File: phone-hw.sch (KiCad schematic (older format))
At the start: 39 parts, among them J1 USB_C_Receptacle_USB2.0, J2 Conn_01x06, J3 Conn_01x05, Q1 S9015, SW1 SW_Push, SW2 SW_Push, SW3 TSWB-3N-CB, U1 ESP32-WROVER, U11 NSI45015WT1G, U2 MCP23008_SO, U3 XC6222B281MR-G, U4 NVT2008, U5 ER-TFT1.44-1, U6 L80-R

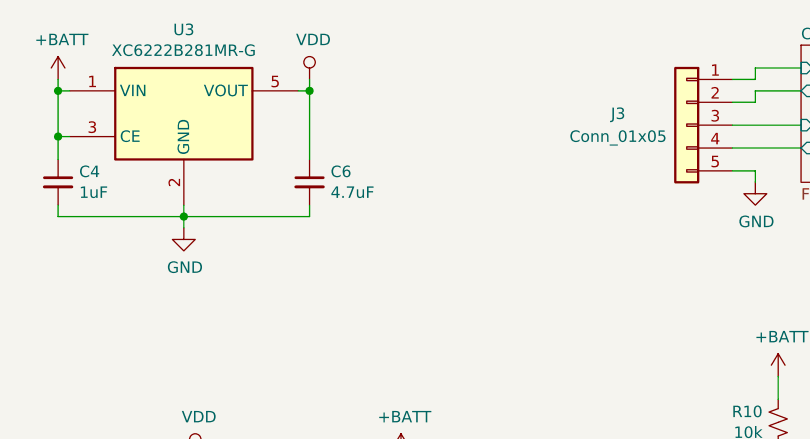
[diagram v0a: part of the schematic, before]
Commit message: add some extra capacitance to the 2.8v line
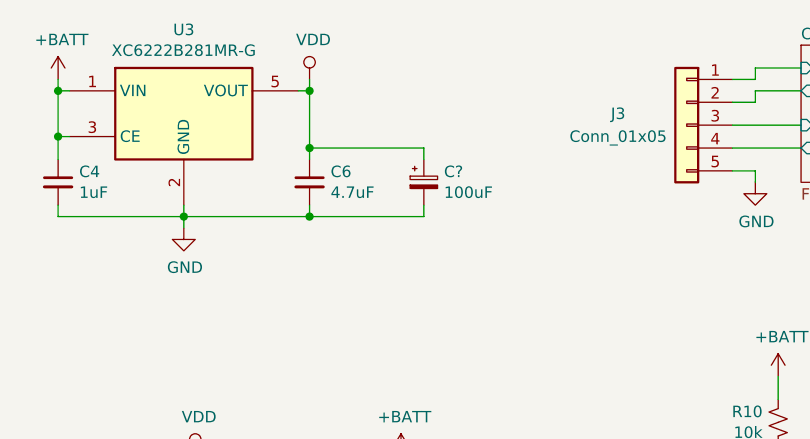
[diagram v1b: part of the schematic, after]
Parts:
- added C?: 100uF, Capacitor_Tantalum_SMD:CP_EIA-3528-15_AVX-H_Pad1.50x2.35mm_HandSolder, symbol Device:CP_Small
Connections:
- net GND: now also C?.2
- net VDD: now also C?.1
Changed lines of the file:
@@
 	6300 1550 6300 1500
 Wire Wire Line
-	6300 1300 6300 1000
+	6300 1300 6300 1250
 Connection ~ 6300 1000
 $Comp
@@
 Wire Wire Line
 	3100 6000 3250 6000
+Wire Wire Line
+	6300 1550 6800 1550
+Wire Wire Line
+	6800 1550 6800 1500
+Connection ~ 6300 1550
+Wire Wire Line
+	6300 1250 6800 1250
+Wire Wire Line
+	6800 1250 6800 1300
+Connection ~ 6300 1250
+Wire Wire Line
+	6300 1250 6300 1000
+$Comp
+L Device:CP_Small C?
+U 1 1 5CE0C170
+P 6800 1400
+F 0 "C?" H 6888 1446 50  0000 L CNN
+F 1 "100uF" H 6888 1355 50  0000 L CNN
+F 2 "Capacitor_Tantalum_SMD:CP_EIA-3528-15_AVX-H_Pad1.50x2.35mm_HandSolder" H 6800 1400 50  0001 C CNN
+F 3 "~" H 6800 1400 50  0001 C CNN
+	1    6800 1400
+	1    0    0    -1
+$EndComp
 $EndSCHEMATC

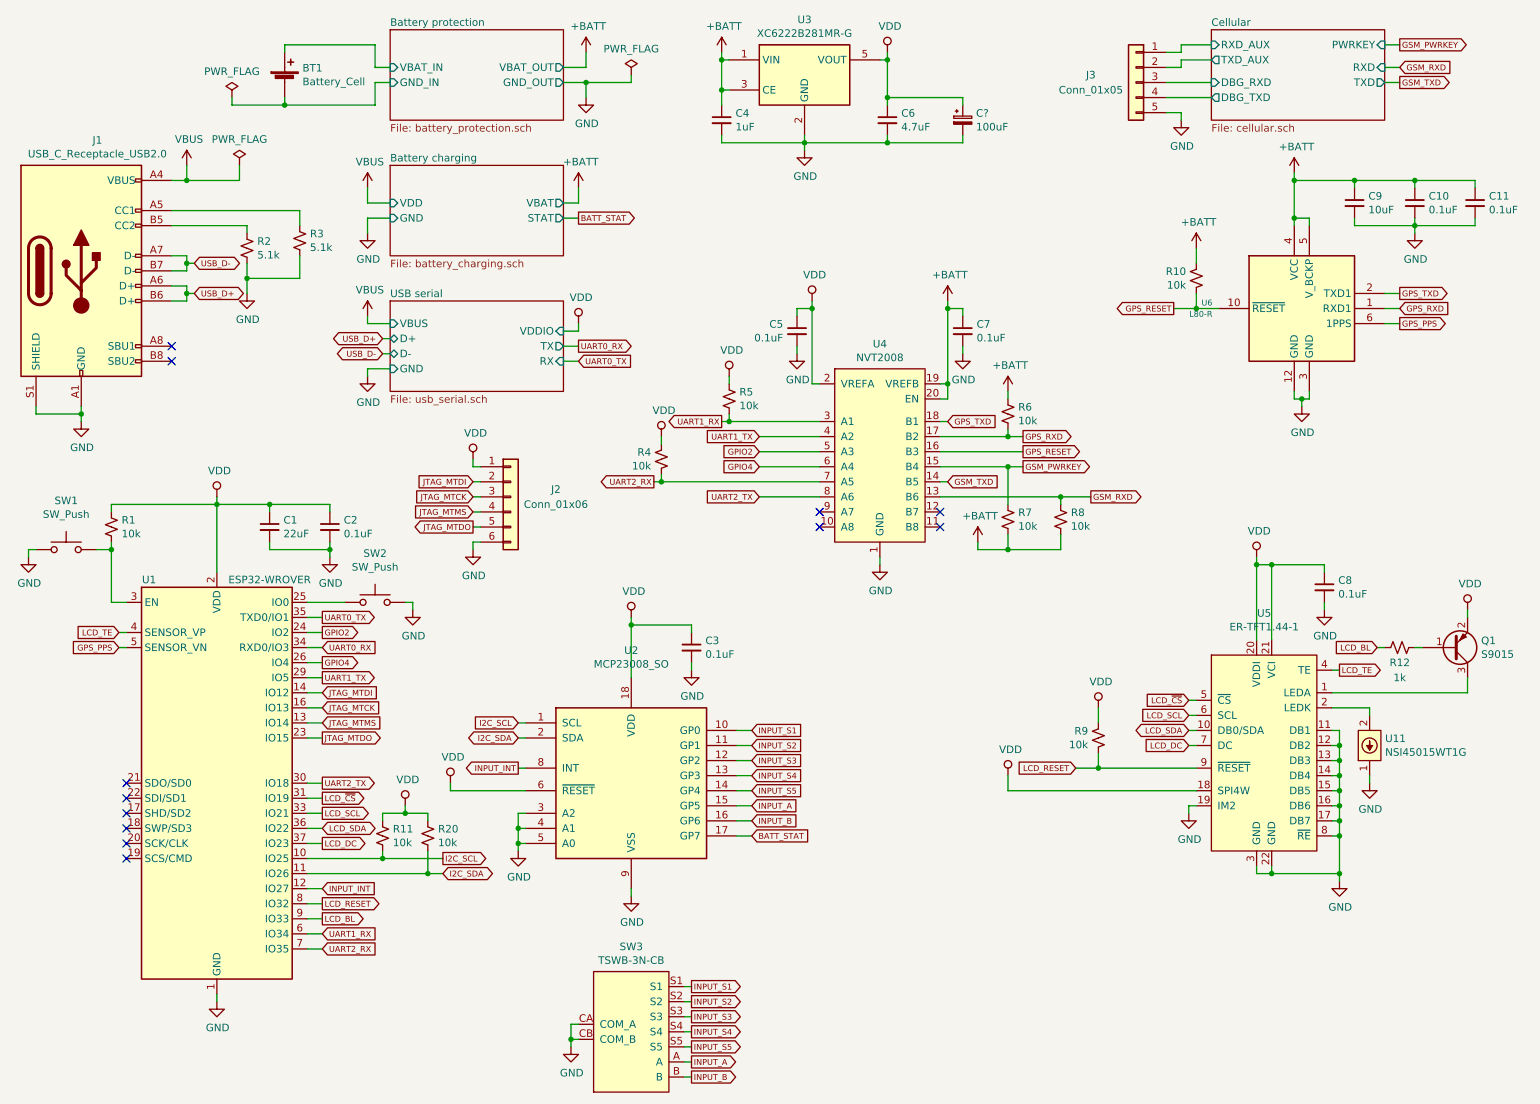
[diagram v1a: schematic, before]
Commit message: clear existing annotations from schematic
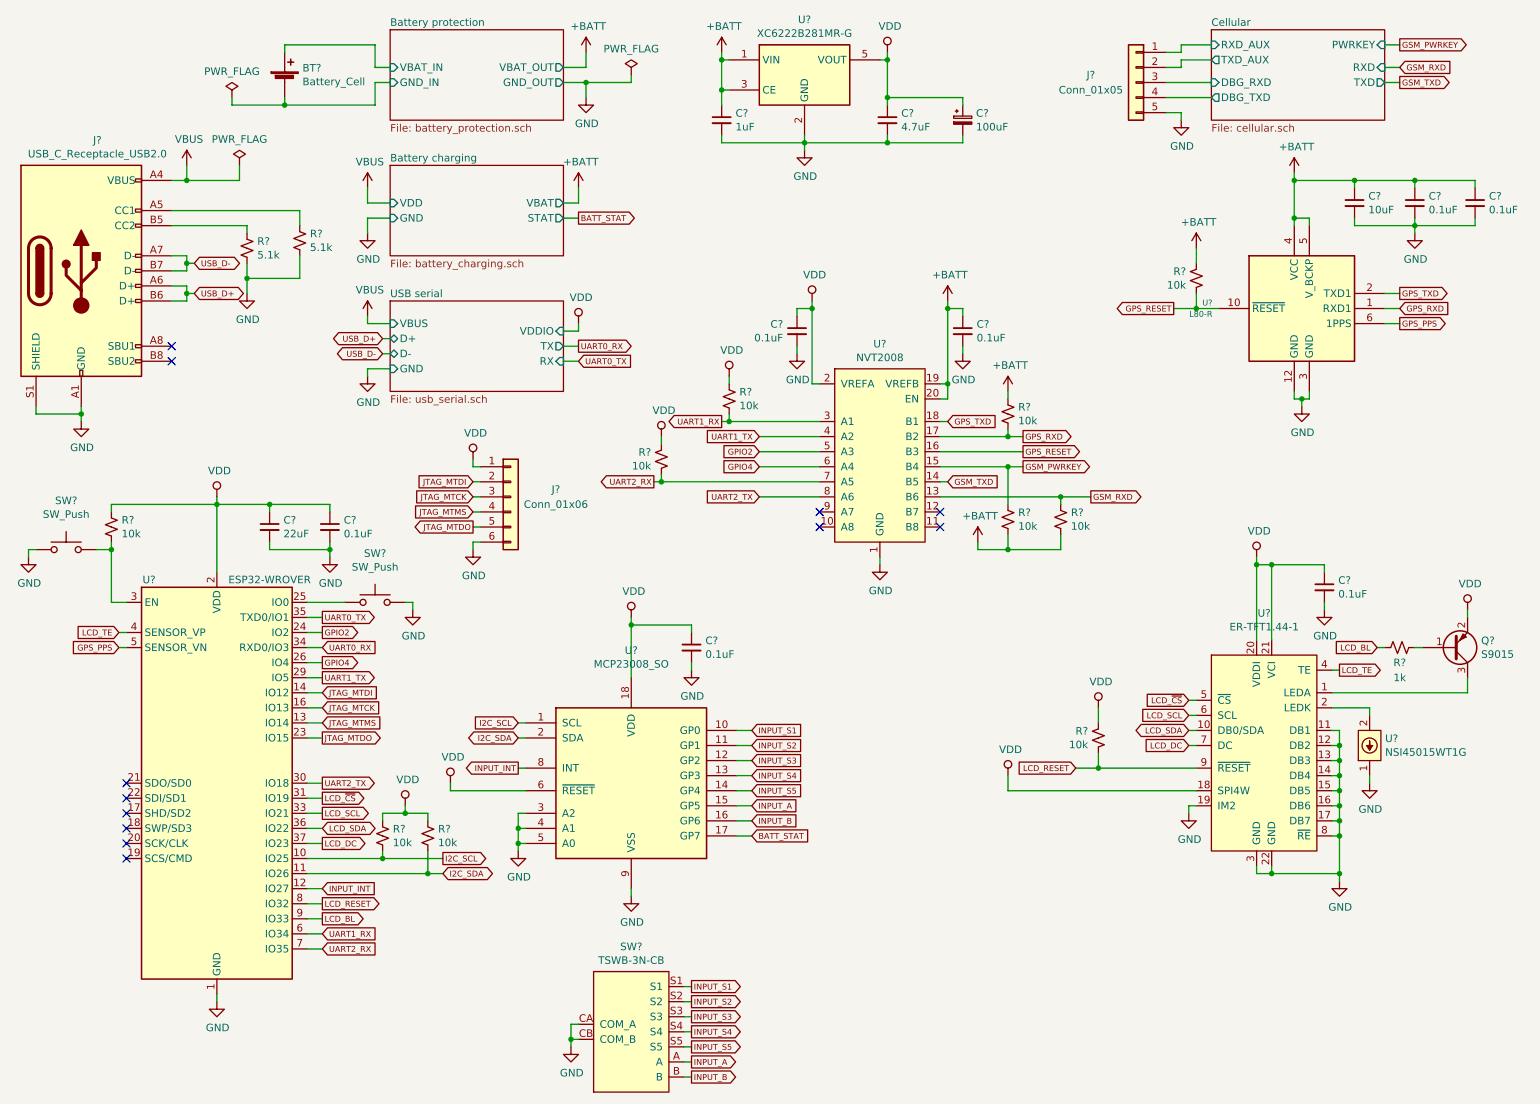
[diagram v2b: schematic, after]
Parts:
- renumbered BT1 to BT?, C4 to C?, C6 to C?, C1 to C?, C2 to C?, C8 to C?, C9 to C?, C10 to C?, C11 to C?, C3 to C?, C5 to C?, C7 to C?, J1 to J?, J3 to J?, J2 to J?, Q1 to Q?, R2 to R?, R3 to R?, R1 to R?, R9 to R?, R10 to R?, R5 to R?, R6 to R?, R7 to R?, R8 to R?, R4 to R?, R12 to R?, R11 to R?, R20 to R?, SW1 to SW?, SW2 to SW?, SW3 to SW?, U3 to U?, U1 to U?, U5 to U?, U4 to U?, U6 to U?, U2 to U?, U11 to U?

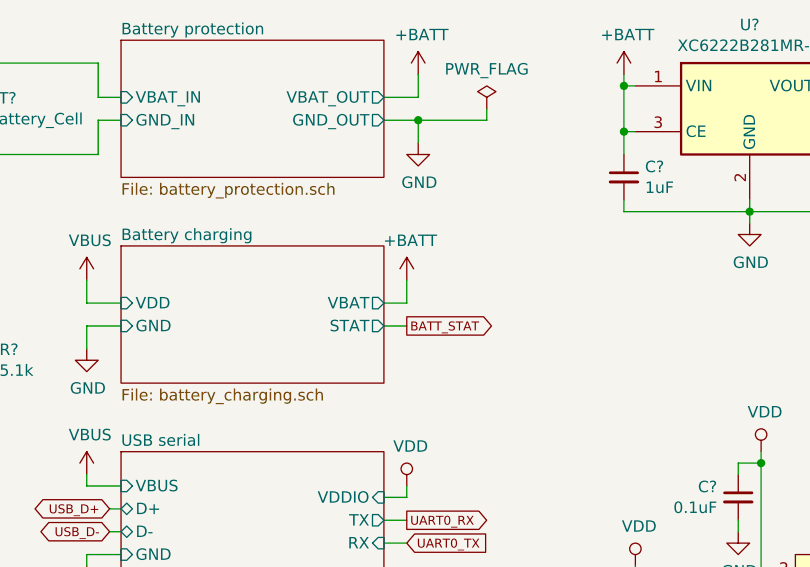
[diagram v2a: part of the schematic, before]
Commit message: fix battery status line to be pulled up to 2.8v, not +vbat
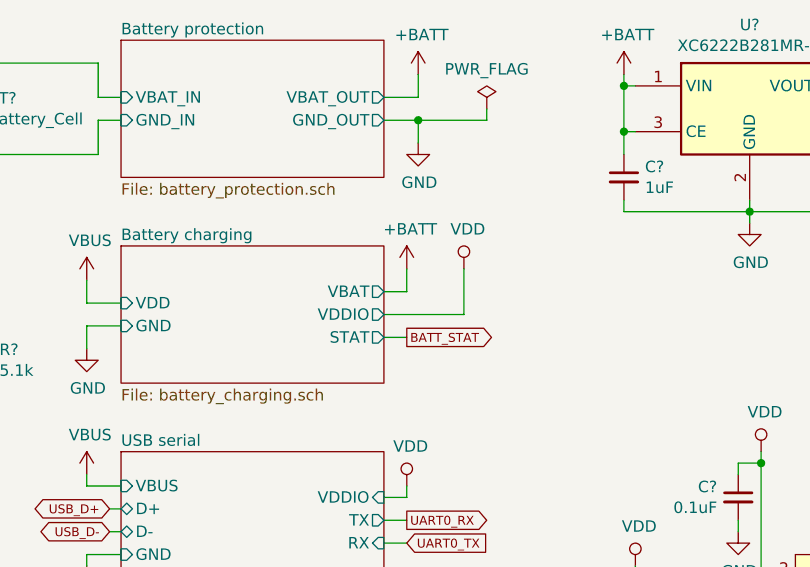
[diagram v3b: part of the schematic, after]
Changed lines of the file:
@@
 F0 "Battery charging" 50
 F1 "battery_charging.sch" 50
-F2 "STAT" O R 4150 2050 50
+F2 "STAT" O R 4150 2100 50
 F3 "VDD" I L 3000 1950 50
-F4 "VBAT" O R 4150 1950 50
+F4 "VBAT" O R 4150 1900 50
 F5 "GND" I L 3000 2050 50
+F6 "VDDIO" O R 4150 2000 50
 $EndSheet
 $Comp
@@
 L power:+BATT #PWR?
 U 1 1 5C93D731
-P 4250 1850
-F 0 "#PWR?" H 4250 1700 50  0001 C CNN
-F 1 "+BATT" H 4265 2023 50  0000 C CNN
-F 2 "" H 4250 1850 50  0001 C CNN
-F 3 "" H 4250 1850 50  0001 C CNN
-	1    4250 1850
-	1    0    0    -1
-$EndComp
-Wire Wire Line
-	4150 1950 4250 1950
-Wire Wire Line
-	4250 1950 4250 1850
-Text GLabel 4250 2050 2    39   Output ~ 0
+P 4250 1800
+F 0 "#PWR?" H 4250 1650 50  0001 C CNN
+F 1 "+BATT" H 4265 1973 50  0000 C CNN
+F 2 "" H 4250 1800 50  0001 C CNN
+F 3 "" H 4250 1800 50  0001 C CNN
+	1    4250 1800
+	1    0    0    -1
+$EndComp
+Wire Wire Line
+	4150 1900 4250 1900
+Wire Wire Line
+	4250 1900 4250 1800
+Text GLabel 4250 2100 2    39   Output ~ 0
 BATT_STAT
 Wire Wire Line
-	4150 2050 4250 2050
+	4150 2100 4250 2100
 $Comp
 L power:GND #PWR?
@@
 	1    0    0    -1
 $EndComp
+$Comp
+L power:VDD #PWR?
+U 1 1 5CE29625
+P 4500 1800
+F 0 "#PWR?" H 4500 1650 50  0001 C CNN
+F 1 "VDD" H 4517 1973 50  0000 C CNN
+F 2 "" H 4500 1800 50  0001 C CNN
+F 3 "" H 4500 1800 50  0001 C CNN
+	1    4500 1800
+	1    0    0    -1
+$EndComp
+Wire Wire Line
+	4150 2000 4500 2000
+Wire Wire Line
+	4500 2000 4500 1800
 $EndSCHEMATC

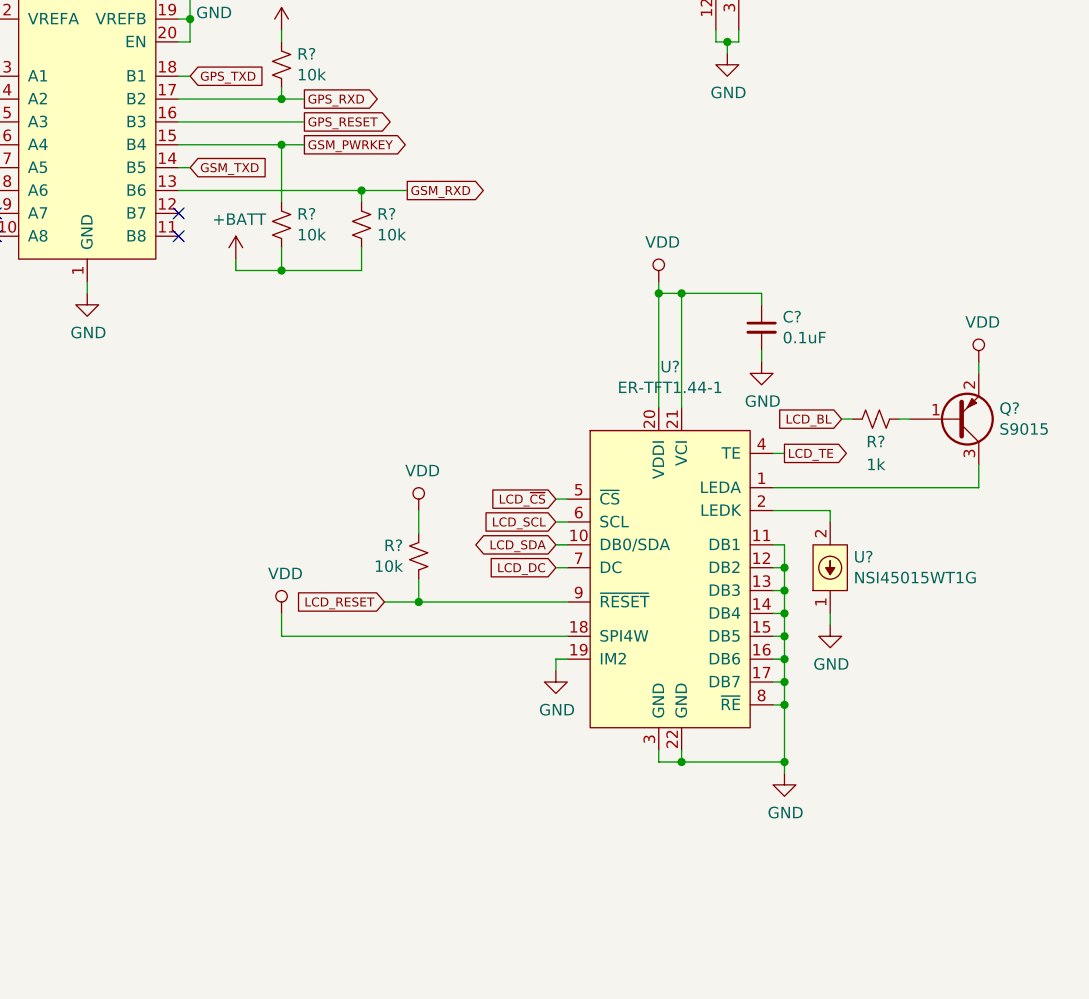
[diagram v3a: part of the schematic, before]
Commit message: fix lcd backlight circuit to use +batt instead of 2.8v for the backlight
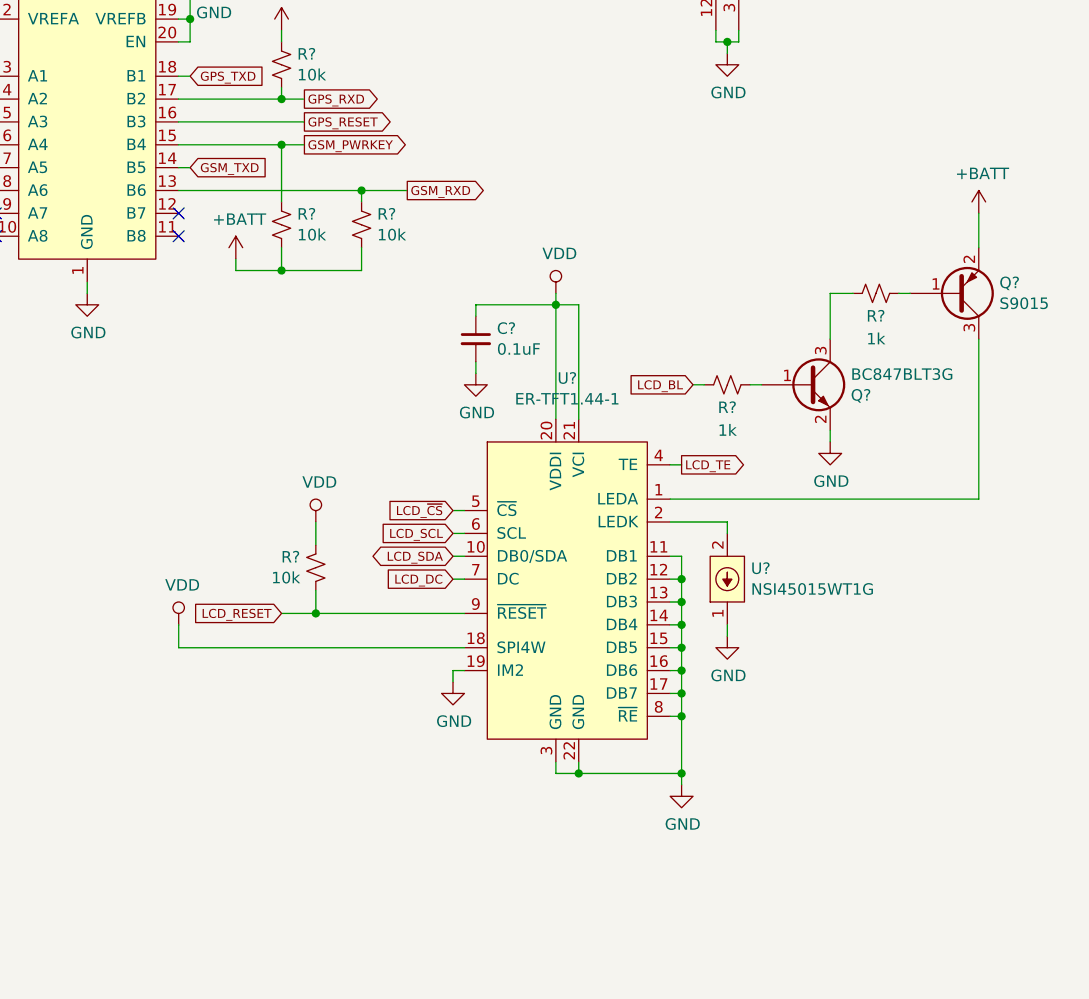
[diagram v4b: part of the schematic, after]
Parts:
- added Q?: BC847BLT3G, Package_TO_SOT_SMD:SOT-23_Handsoldering, symbol Device:Q_NPN_BEC
- added R?: 1k, Resistor_SMD:R_0603_1608Metric_Pad1.05x0.95mm_HandSolder, symbol Device:R_Small_US
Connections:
- net +BATT: now also Q?.2 (E)
- net GND: now also Q?.2 (E)
- net LCD_BL: now also R?.2; no longer R?.2
- net VDD: no longer Q?.2 (E)
- new net: Q?.1 (B), R?.1
- new net: Q?.3 (C), R?.2
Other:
- moved on the sheet: C?, Q?, R?, U?
